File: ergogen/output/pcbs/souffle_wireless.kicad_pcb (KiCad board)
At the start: 2 copper layers, 134.9 x 109.8 mm, 128 parts

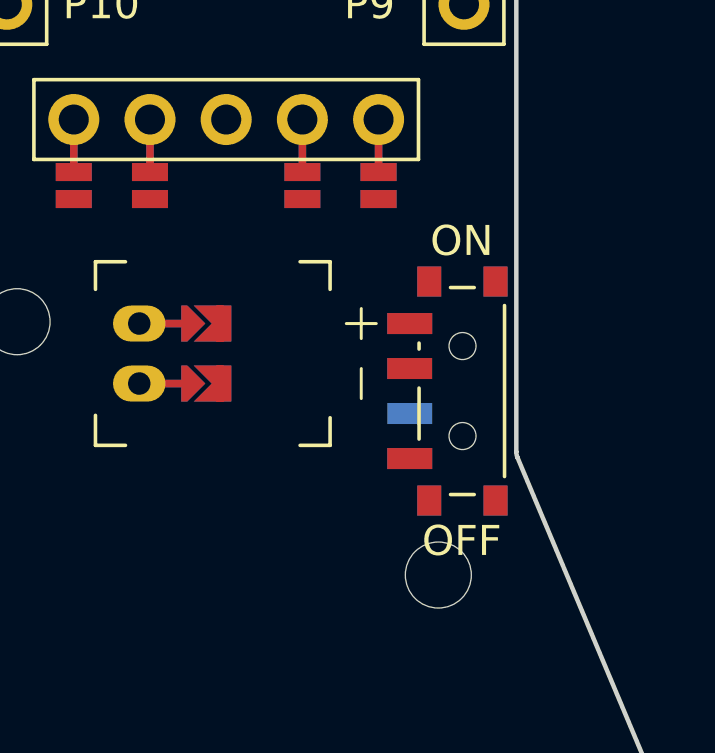
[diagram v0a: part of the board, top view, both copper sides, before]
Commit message: feat: moved on off switch a bit up
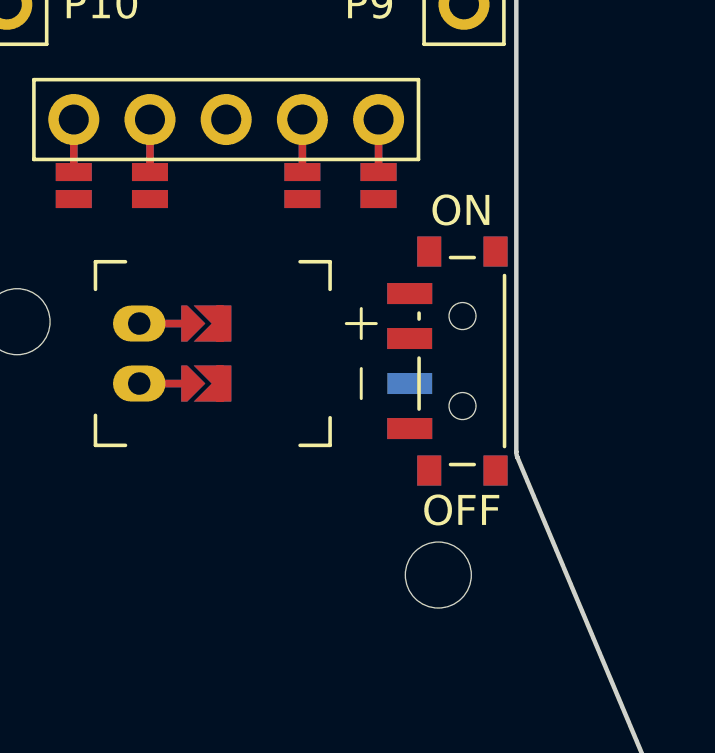
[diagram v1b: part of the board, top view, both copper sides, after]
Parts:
- moved PWR1 1.00 mm to (219.8, 101.8)
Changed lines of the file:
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@@
   (footprint "ceoloide:power_switch_smd_side"
     (layer "F.Cu")
-    (at 219.75 102.75 0)
+    (at 219.75 101.75 0)
     (property "Reference" "PWR1"
       (at -3.6 0 -90)

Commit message: feat: revert moving on off switch
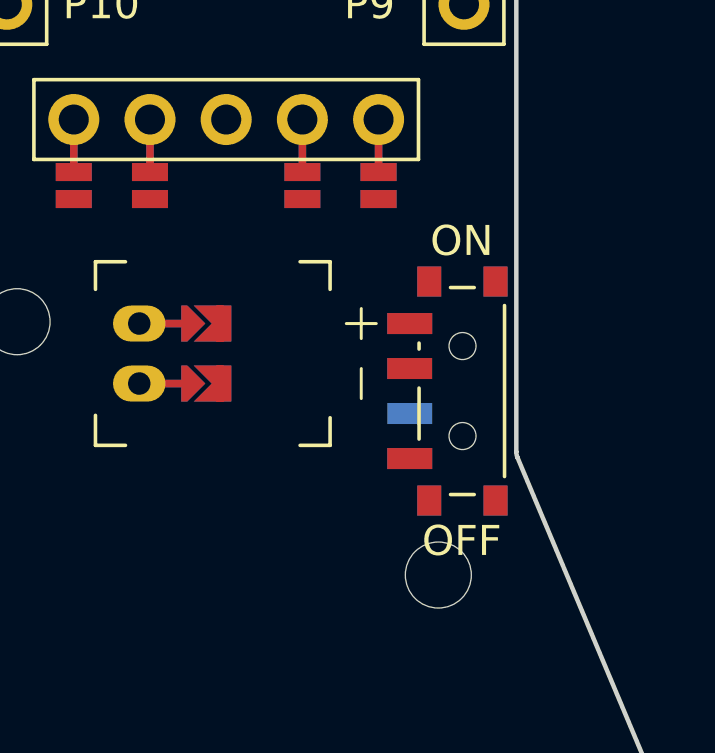
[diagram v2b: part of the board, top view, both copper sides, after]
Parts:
- moved PWR1 1.00 mm to (219.8, 102.8)
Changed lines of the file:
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@@
   (footprint "ceoloide:power_switch_smd_side"
     (layer "F.Cu")
-    (at 219.75 101.75 0)
+    (at 219.75 102.75 0)
     (property "Reference" "PWR1"
       (at -3.6 0 -90)
